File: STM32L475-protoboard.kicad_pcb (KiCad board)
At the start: 4 copper layers, 73.6 x 55.9 mm, 93 parts, among them J1 USB_HEADER, J10 BOOT_MODE, J11 PAD_PB4, J12 PAD_PB5, J13 PAD_PC4, J14 PAD_PC5, J15 PAD_GND, J16 Conn_02x20_Odd_Even, J17 3v3-hdr, J2 USB_B_Micro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

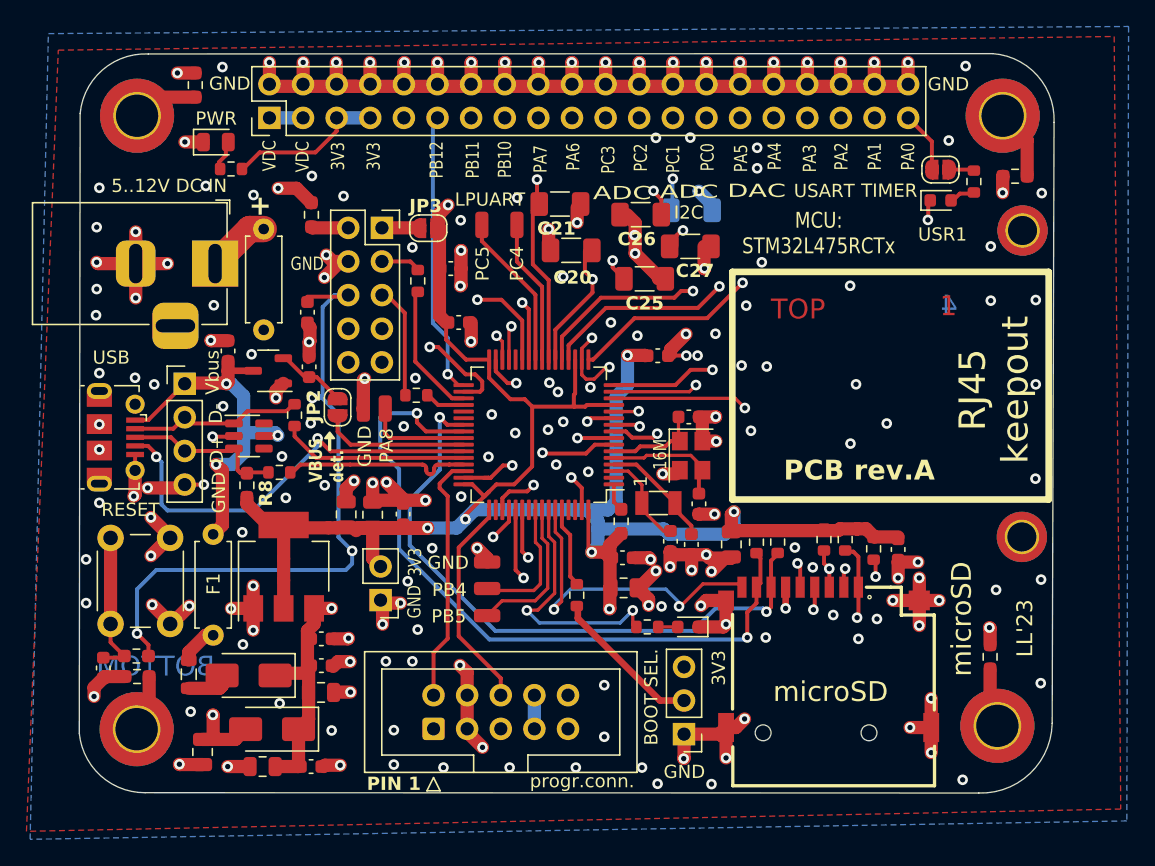
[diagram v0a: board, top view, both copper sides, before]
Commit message: mounting holes
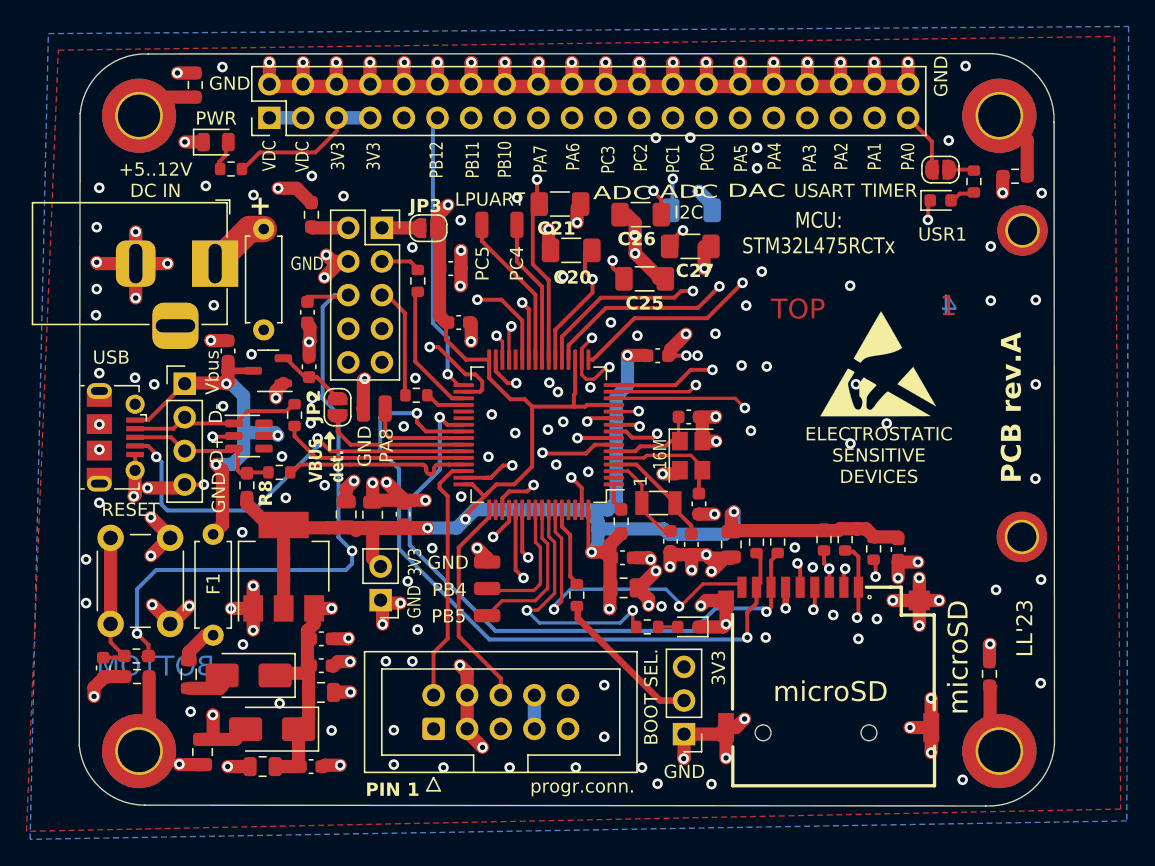
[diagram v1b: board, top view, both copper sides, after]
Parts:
- added REF**: ESD-Logo_8.9x8mm_SilkScreen, Symbol:ESD-Logo_8.9x8mm_SilkScreen, F.Cu at (127.2, 72.7)
- moved REF** 42.3 mm to (123.8, 66.5)
- moved H6 1.91 mm to (136.3, 102.0)
- moved H3 1.66 mm to (71.3, 102.0)
- moved R20 1.29 mm to (135.6, 96.1)
- moved H5 0.25 mm to (136.3, 54.0)
- moved H4 0.15 mm to (71.3, 54.0)
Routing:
- net Net-(H6-Pad1): track 4.53 -> 3.26 mm
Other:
- board size 73.6 x 55.9 mm -> 73.7 x 56.8 mm
- board text added: "+5..12V DC IN"
- board text removed: "5..12V DC IN"
- board text removed: "RJ45 keepout"

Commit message: drc trace separtion checking
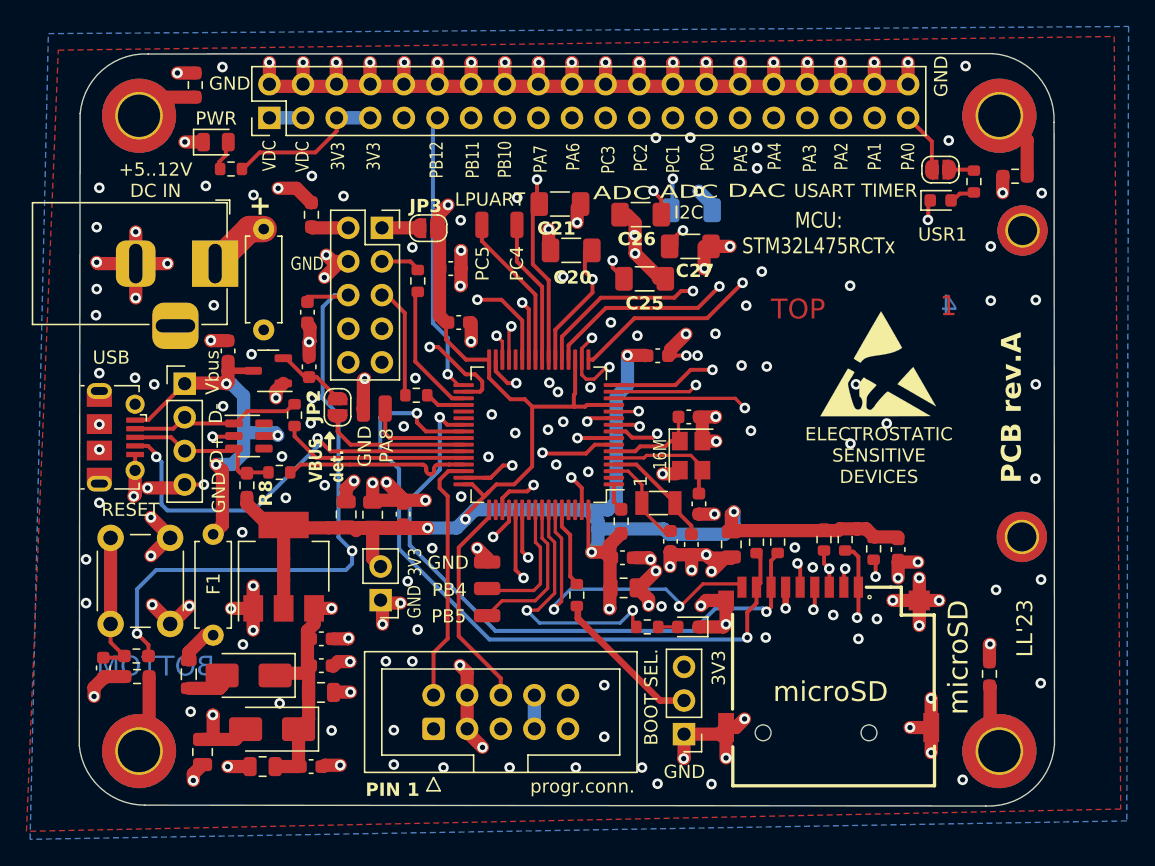
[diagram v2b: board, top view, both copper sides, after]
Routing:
- net Net-(H3-Pad1): track 4.37 -> 5.95 mm
- net GND: track 259.7 -> 260.9 mm, vias 202 -> 203
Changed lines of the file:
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@@
   (segment (start 93.85 49.925) (end 93.85 51.735) (width 1) (layer "F.Cu") (net 1))
   (segment (start 109.825 87.35) (end 108.775 87.35) (width 1) (layer "F.Cu") (net 1))
-  (segment (start 74.35 102.95) (end 74.375 102.975) (width 1) (layer "F.Cu") (net 1))
   (segment (start 88.75 49.925) (end 88.75 51.715) (width 1) (layer "F.Cu") (net 1))
   (segment (start 86.51 64.965) (end 85.3 66.175) (width 1) (layer "F.Cu") (net 1))
@@
   (segment (start 130.25 90.575) (end 130.25 88.875) (width 1) (layer "F.Cu") (net 1))
   (segment (start 116.05 87.375) (end 115.55 87.375) (width 1) (layer "F.Cu") (net 1))
+  (segment (start 75.4 104.175) (end 75.4 103.675) (width 1) (layer "F.Cu") (net 1))
   (segment (start 106.55 51.735) (end 106.55 49.925) (width 1) (layer "F.Cu") (net 1))
   (segment (start 98.25 72.38) (end 98.25 73.255361) (width 0.3) (layer "F.Cu") (net 1))
@@
   (segment (start 96.39 49.935) (end 96.4 49.925) (width 1) (layer "F.Cu") (net 1))
   (segment (start 96.4 70.985) (end 96.38 71.005) (width 1) (layer "F.Cu") (net 1))
+  (segment (start 75.4 103.675) (end 76.1 102.975) (width 1) (layer "F.Cu") (net 1))
   (segment (start 83.7 49.925) (end 83.7 51.725) (width 1) (layer "F.Cu") (net 1))
   (segment (start 78.4125 78.2) (end 78.4625 78.15) (width 0.3) (layer "F.Cu") (net 1))
@@
   (segment (start 113.05 88.275) (end 113.05 87.14) (width 1) (layer "F.Cu") (net 1))
   (segment (start 101.47 51.735) (end 101.47 49.955) (width 1) (layer "F.Cu") (net 1))
+  (segment (start 114.5125 63.825) (end 115.95 63.825) (width 1) (layer "F.Cu") (net 1))
   (segment (start 74.755 81.825) (end 74.75 81.82) (width 0.3) (layer "F.Cu") (net 1))
   (segment (start 96.4 69.575) (end 96.4 70.985) (width 1) (layer "F.Cu") (net 1))
@@
   (segment (start 136.55 58.55) (end 136.575 58.525) (width 1) (layer "F.Cu") (net 1))
   (segment (start 111.63 49.945) (end 111.65 49.925) (width 1) (layer "F.Cu") (net 1))
-  (segment (start 74.375 102.975) (end 76.1 102.975) (width 1) (layer "F.Cu") (net 1))
   (segment (start 97.8666 81.3084) (end 97.7034 81.3084) (width 0.3) (layer "F.Cu") (net 1))
   (segment (start 86.2 51.705) (end 86.23 51.735) (width 1) (layer "F.Cu") (net 1))
@@
   (via (at 139.5 59.8) (size 0.8) (drill 0.4) (layers "F.Cu" "B.Cu") (free) (net 1))
   (via (at 87.125 93.425) (size 0.8) (drill 0.4) (layers "F.Cu" "B.Cu") (free) (net 1))
-  (via (at 74.35 102.95) (size 0.8) (drill 0.4) (layers "F.Cu" "B.Cu") (free) (net 1))
+  (via (at 75.4 104.175) (size 0.8) (drill 0.4) (layers "F.Cu" "B.Cu") (free) (net 1))
   (via (at 112.65 72.075) (size 0.8) (drill 0.4) (layers "F.Cu" "B.Cu") (net 1))
   (via (at 114.87 76.695) (size 0.8) (drill 0.4) (layers "F.Cu" "B.Cu") (free) (net 1))
@@
   (via (at 87.249 95.1992) (size 0.8) (drill 0.4) (layers "F.Cu" "B.Cu") (free) (net 1))
   (via (at 114.02 65.485) (size 0.8) (drill 0.4) (layers "F.Cu" "B.Cu") (net 1))
+  (via (at 115.95 63.825) (size 0.8) (drill 0.4) (layers "F.Cu" "B.Cu") (free) (net 1))
   (via (at 111.65 49.925) (size 0.8) (drill 0.4) (layers "F.Cu" "B.Cu") (free) (net 1))
   (via (at 68.1 62.375) (size 0.8) (drill 0.4) (layers "F.Cu" "B.Cu") (free) (net 1))
@@
   (segment (start 91.38 68.855) (end 90.03 67.505) (width 0.3) (layer "F.Cu") (net 8))
   (segment (start 90.03 67.505) (end 89.65 67.505) (width 0.3) (layer "F.Cu") (net 8))
+  (segment (start 94.01 82.085) (end 94.01 81.465) (width 0.3) (layer "F.Cu") (net 9))
+  (segment (start 94.01 81.465) (end 94.6666 80.8084) (width 0.3) (layer "F.Cu") (net 9))
+  (segment (start 94.94964 80.805) (end 95.825 80.805) (width 0.3) (layer "F.Cu") (net 9))
   (segment (start 94.62 93.455) (end 94.62 82.695) (width 0.3) (layer "F.Cu") (net 9))
   (segment (start 93.55 97.735) (end 93.55 94.525) (width 0.3) (layer "F.Cu") (net 9))
-  (segment (start 94.01 81.744639) (end 94.949639 80.805) (width 0.3) (layer "F.Cu") (net 9))
+  (segment (start 94.6666 80.8084) (end 94.94624 80.8084) (width 0.3) (layer "F.Cu") (net 9))
+  (segment (start 94.94624 80.8084) (end 94.94964 80.805) (width 0.3) (layer "F.Cu") (net 9))
   (segment (start 94.62 82.695) (end 94.01 82.085) (width 0.3) (layer "F.Cu") (net 9))
-  (segment (start 94.949639 80.805) (end 95.825 80.805) (width 0.3) (layer "F.Cu") (net 9))
   (segment (start 93.55 94.525) (end 94.62 93.455) (width 0.3) (layer "F.Cu") (net 9))
-  (segment (start 94.01 82.085) (end 94.01 81.744639) (width 0.3) (layer "F.Cu") (net 9))
   (segment (start 95.45 86.575) (end 95.45 93.275) (width 0.3) (layer "F.Cu") (net 10))
   (segment (start 98.63 96.455) (end 98.63 97.735) (width 0.3) (layer "F.Cu") (net 10))
@@
   (segment (start 102.175 86.3) (end 101.75 85.875) (width 0.25) (layer "F.Cu") (net 25))
   (segment (start 102.175 89.65) (end 102.175 86.3) (width 0.25) (layer "F.Cu") (net 25))
-  (segment (start 72.0625 99.3575) (end 71.12 100.3) (width 1) (layer "F.Cu") (net 26))
-  (segment (start 72.0625 96.325) (end 72.0625 99.3575) (width 1) (layer "F.Cu") (net 26))
+  (segment (start 72.0625 96.325) (end 72.0625 101.1925) (width 1) (layer "F.Cu") (net 26))
+  (segment (start 72.0625 101.1925) (end 71.3 101.955) (width 1) (layer "F.Cu") (net 26))
   (segment (start 72.555 52.55) (end 71.15 53.955) (width 1) (layer "F.Cu") (net 27))
   (segment (start 75.55 52.55) (end 72.555 52.55) (width 1) (layer "F.Cu") (net 27))

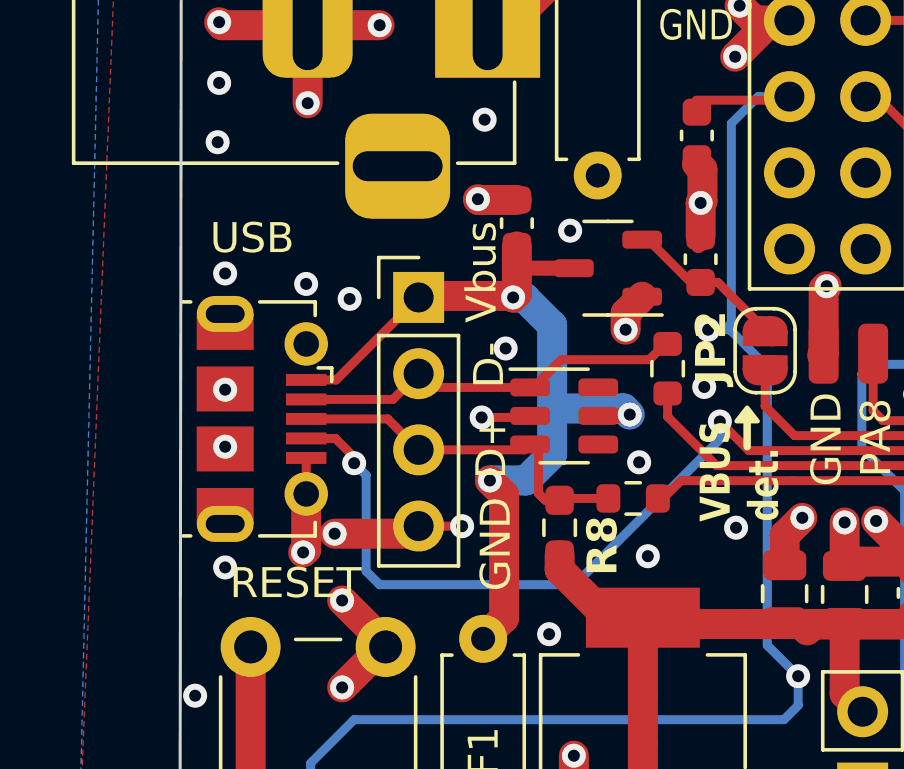
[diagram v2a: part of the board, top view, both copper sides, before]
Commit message: micro usb connector change
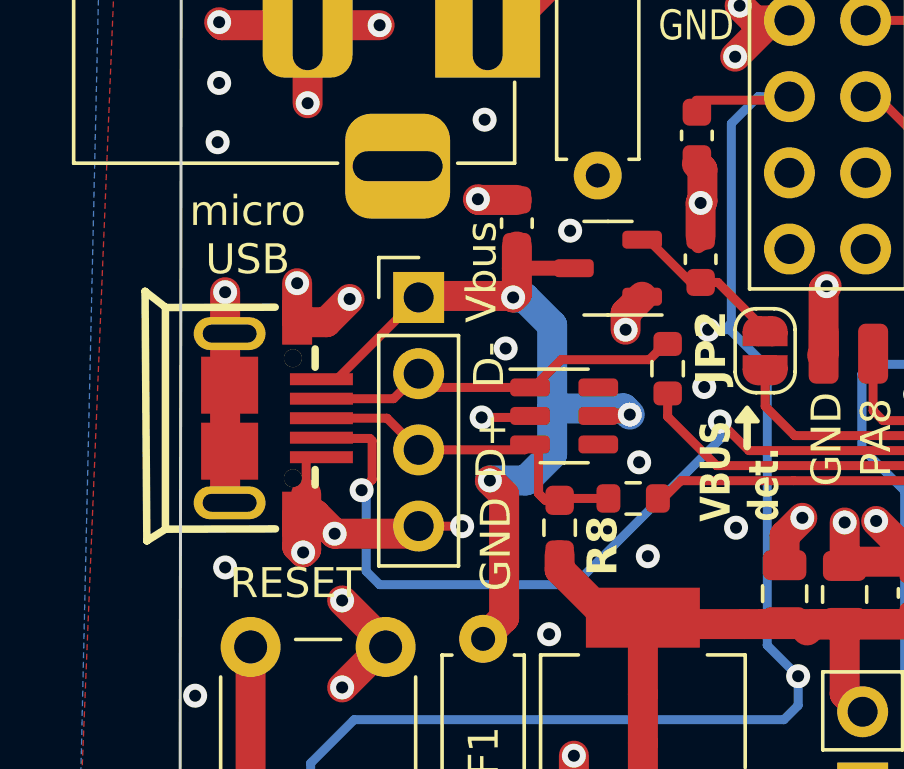
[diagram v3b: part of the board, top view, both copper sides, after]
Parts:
- removed J2: USB_B_Micro, Connector_USB:USB_Micro-B_Molex-105017-0001
- added USB1: MICRO5.9MMUSB, STM32L475-protoboard:MICRO-USB-SMD_5P-P0.65-H-F_MICRO5.9MMUSB, F.Cu at (70.0, 78.2)
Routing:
- net GND: track 260.9 -> 274.2 mm, vias 203 -> 201
- net PA10: track 31.8 -> 32.8 mm
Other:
- board text added: "micro USB"

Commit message: forgotted microUSB files + silk modifications to pcb
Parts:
- moved REF** 1.01 mm to (124.2, 65.6)
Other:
- board text added: "ARM® Cortex®-M4 32bit 256KB flash, 128KB SRAM"
- board text added: "MCU: STM32L475RCT6"
- board text removed: "MCU: STM32L475RCTx"
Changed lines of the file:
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@@
     (pad "6" smd rect (at 3.2 -0.72 270) (size 1.5 1) (layers "F.Cu" "F.Paste" "F.Mask")
       (net 1 "GND") (pinfunction "6") (pintype "unspecified"))
-    (model "${EASYEDA2KICAD}/easyeda2kicad.3dshapes/MICRO-USB-SMD_MICRO5.9MMUSB.wrl"
-      (offset (xyz 0 -1.5 1.5))
+    (model "${KIPRJMOD}/MICRO-USB-SMD_MICRO5.9MMUSB.wrl"
+      (offset (xyz 0 -1.5 0))
       (scale (xyz 1 1 1))
       (rotate (xyz 0 0 180))
@@
   )
   (footprint "Symbol:ESD-Logo_8.9x8mm_SilkScreen" locked (layer "B.Cu")
-    (at 123.8 66.475 180)
+    (at 124.25 65.575 180)
     (descr "Electrostatic discharge Logo")
     (tags "Logo ESD")
@@
     (effects (font (size 1 1) (thickness 0.25)) (justify mirror))
   )
+  (gr_text "ARM® Cortex®-M4 32bit\n256KB flash, 128KB SRAM" (at 134.9 83.525) (layer "B.SilkS")
+    (effects (font (size 1 1) (thickness 0.25) bold) (justify left bottom mirror))
+  )
   (gr_text "GND" (at 115.65 100.675) (layer "B.SilkS")
     (effects (font (size 1 1) (thickness 0.25)) (justify mirror))
@@
     (effects (font (size 1 0.8) (thickness 0.2)) (justify mirror))
   )
-  (gr_text "MCU:\nSTM32L475RCTx" (at 135.6 79.375) (layer "B.SilkS")
-    (effects (font (size 2 2) (thickness 0.4) bold) (justify left mirror))
+  (gr_text "MCU:\nSTM32L475RCT6" (at 134.9 77.525) (layer "B.SilkS")
+    (effects (font (size 1.5 1.5) (thickness 0.375) bold) (justify left mirror))
   )
   (gr_text "GND" (at 131.95 51.025 90) (layer "B.SilkS")
@@
     (effects (font (size 1 1) (thickness 0.25)) (justify mirror))
   )
-  (gr_text "ELECTROSTATIC\nSENSITIVE\nDEVICES" (at 123.75 73.425) (layer "B.SilkS")
+  (gr_text "ELECTROSTATIC\nSENSITIVE\nDEVICES" (at 124.2 72.525) (layer "B.SilkS")
     (effects (font (size 1 1) (thickness 0.25)) (justify mirror))
   )
@@
     (effects (font (size 1 1) (thickness 0.25)))
   )
-  (gr_text "MCU: \nSTM32L475RCTx" (at 122.65 62.825) (layer "F.SilkS" knockout)
+  (gr_text "MCU: \nSTM32L475RCT6" (at 122.65 62.825) (layer "F.SilkS" knockout)
     (effects (font (size 1.2 1) (thickness 0.25)))
   )
